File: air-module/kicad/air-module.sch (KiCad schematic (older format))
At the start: 38 parts, among them J1 IDC12, J2 ARM_SWD_SMALL, P1 USB_OTG, U1 Alphasense_OPC-N2, U2 nRF52832, U3 Plantower_PM2.5_PMS_5003, U4 TPS2064, U5 BME280, U6 TPS79133

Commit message: Fixes #1
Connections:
- net MCU-RX: now also R10.1; no longer R7.1
- net MCU-TX: now also R7.1; no longer R10.1
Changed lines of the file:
@@
 NoConn ~ 4900 1750
 NoConn ~ 4900 2050
+Text GLabel 5575 2050 2    60   Input ~ 0
+MCU-RX
 Text GLabel 5575 1525 2    60   Input ~ 0
-MCU-RX
-Text GLabel 5575 2050 2    60   Input ~ 0
 MCU-TX
 Text GLabel 5575 1875 2    60   Input ~ 0

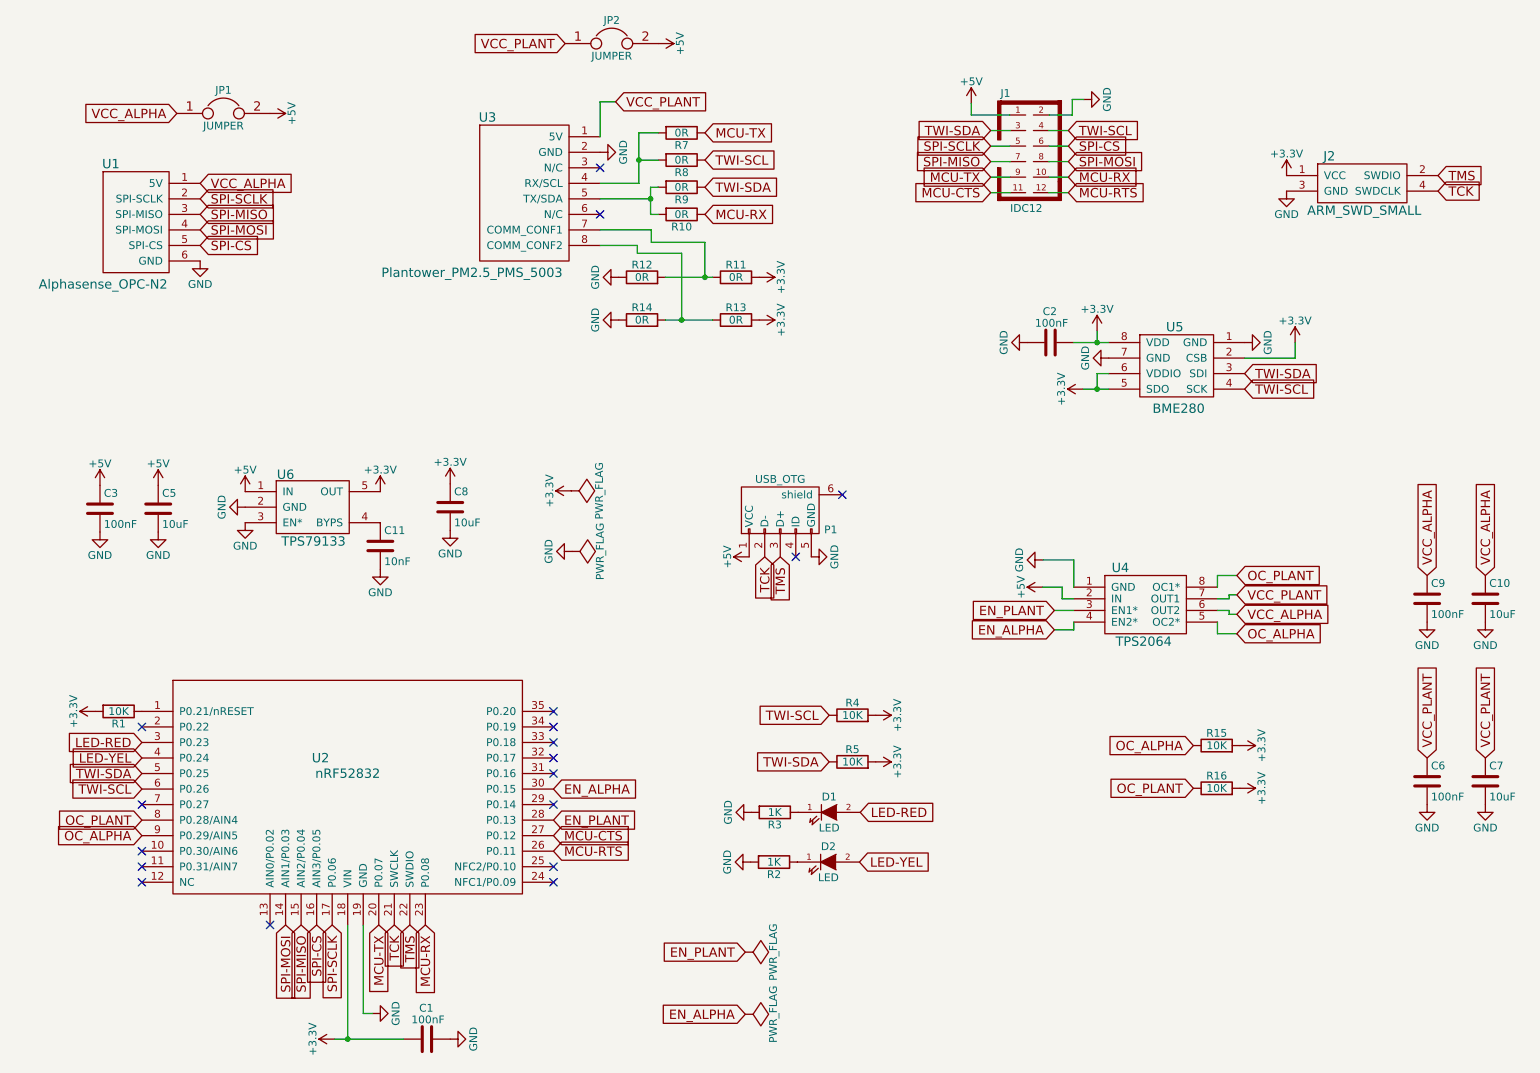
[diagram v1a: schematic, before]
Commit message: Air Module PCB update, Fixes #4, Fixes #5, Fixes #6, Fixes #7, Fixes #8
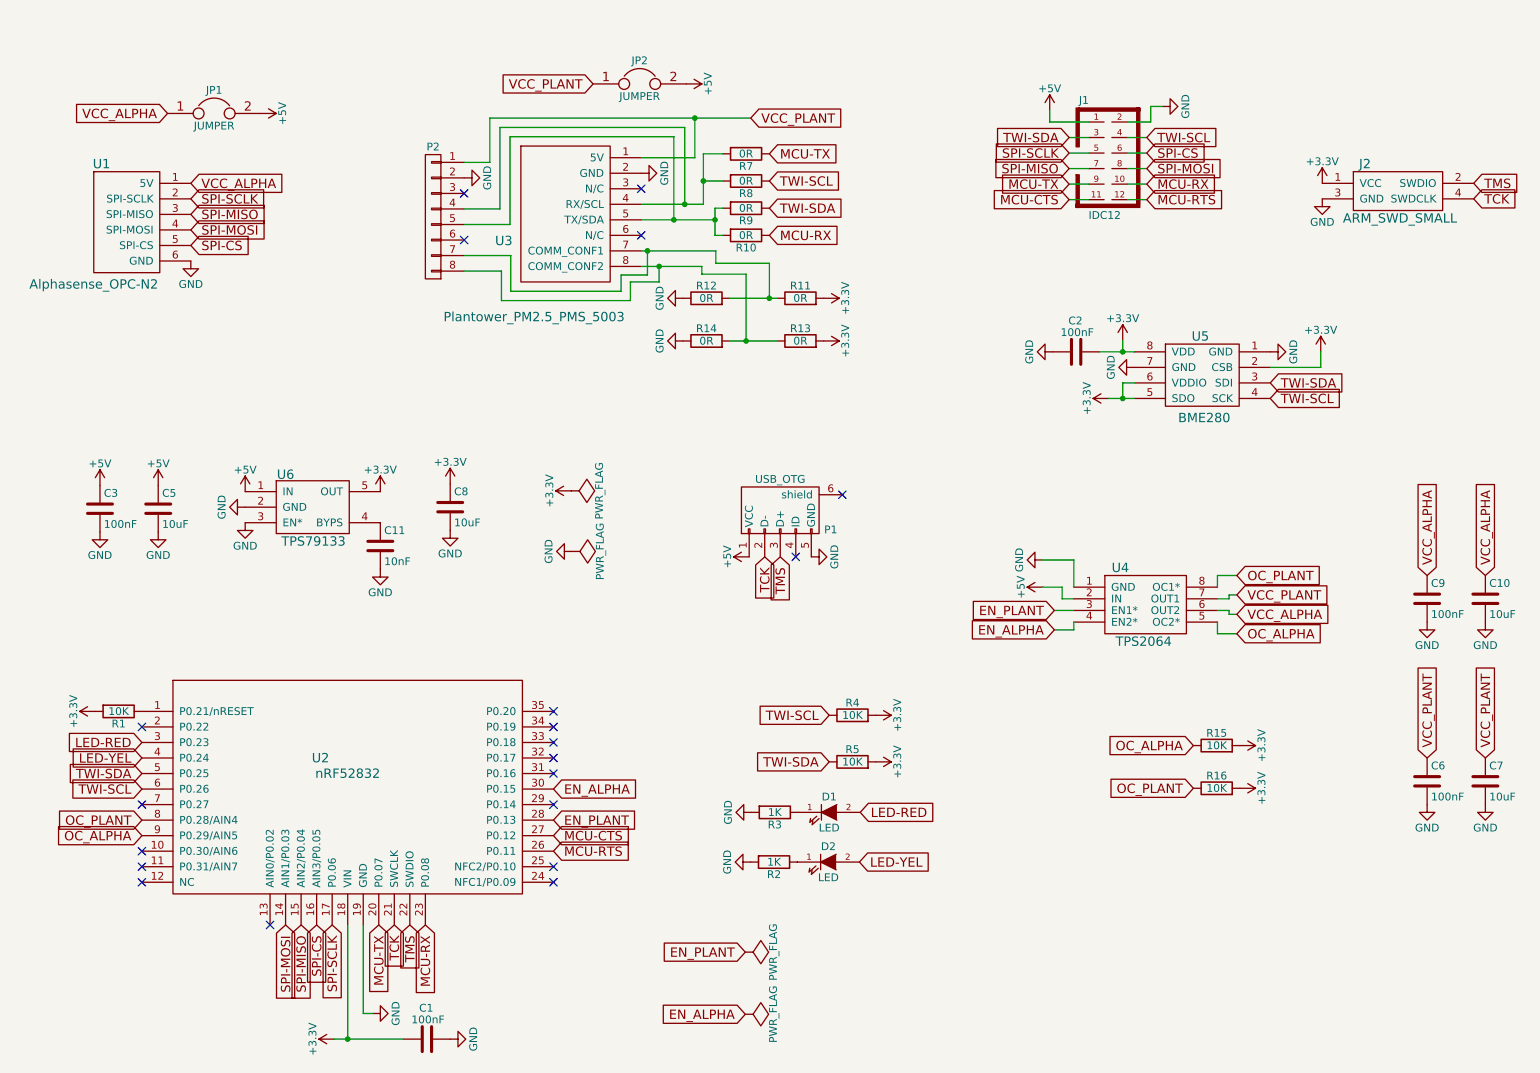
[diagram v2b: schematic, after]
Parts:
- added P2: CONN_01X08, Molex-53047-0810:Molex-53047-0810, symbol CONN_01X08
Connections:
- net GND: now also P2.2 (P2)
- net VCC_PLANT: now also P2.1 (P1)
- net at R7.2, R8.2, U3.4 (RX/SCL): now also P2.4 (P4)
- net at R10.2, R9.2, U3.5 (TX/SDA): now also P2.5 (P5)
- net at R11.1, R12.2, U3.7 (COMM_CONF1): now also P2.7 (P7)
- net at R13.1, R14.2, U3.8 (COMM_CONF2): now also P2.8 (P8)
- no-connect marks 18 -> 20
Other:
- moved on the sheet: C2, J1, J2, JP1, JP2, R10, R11, R12, R13, R14, R7, R8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
